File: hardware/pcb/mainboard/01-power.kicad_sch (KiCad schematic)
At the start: 42 parts, among them J1 BATTERIE JST-PH, J2 BOUTON contact JST-PH, J3 BOUTON LED JST-PH, Q1 AO3401A, Q2 2N7002, Q3 2N7002, SW1 QON, U2 BQ25896RTW, U3 TPS63001DRCR, U4 TPS61023DRL

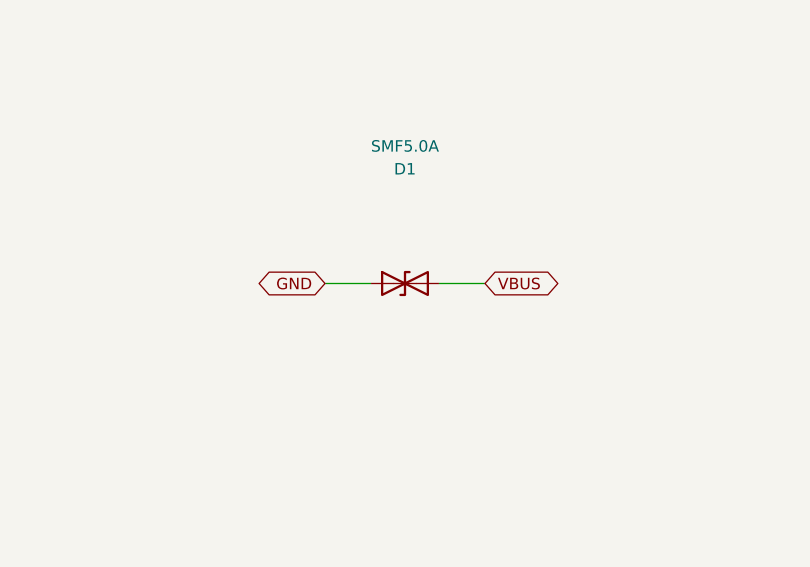
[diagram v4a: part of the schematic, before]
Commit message: fix(pcb): turn the VBUS TVS the right way round on both boards
D1 (SMF5.0A, unidirectional) carried Device:D_TVS, KiCad's bidirectional
symbol. Its pins are A1/A2, so no polarity is expressed, ERC has nothing to
reject, and the cathode landed wherever the wire ran — on GND. Plugging in
USB-C would have forward-biased the diode straight across VBUS, shorting the
port it protects.

Both boards now use Device:D_Zener, pin 1 = K, cathode on VBUS. The footprint
is rotated 180° so the symmetric SOD-123 pads keep the same copper: no track
moves, and DRC and unconnected counts are identical before and after.

check_pcb.py gains control H3 — every D<n> footprint must carry K/A pads. It
fails on the boards as they stood and passes 4/4 on the corrected ones.

Co-Authored-By: Claude Opus 5 (1M context) <noreply@anthropic.com>
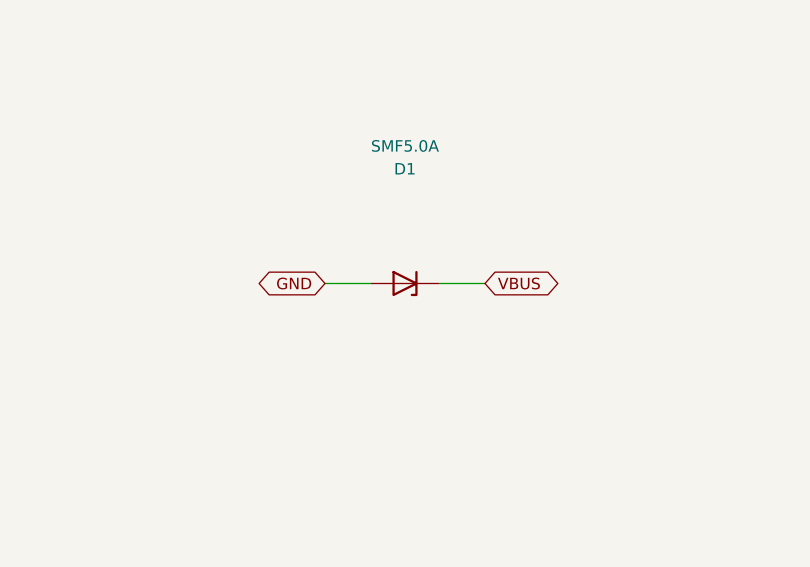
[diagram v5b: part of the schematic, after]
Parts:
- D1: symbol Device:D_TVS -> Device:D_Zener
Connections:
- net GND: now also D1.2 (A); no longer D1.1 (A1)
- net VBUS: now also D1.1 (K); no longer D1.2 (A2)
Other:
- moved on the sheet: D1
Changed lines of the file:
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@@
 	)
 	(symbol
-		(lib_id "Device:D_TVS")
-		(at 229.87 133.35 0)
+		(lib_id "Device:D_Zener")
+		(at 229.87 133.35 180)
 		(unit 1)
 		(body_style 1)
@@
 			)
 		)
-		(property "Description" ""
+		(property "Description" "TVS unidirectionnelle 5 V. Symbole zener parce que Device:D_TVS est bidirectionnel : ses broches A1/A2 n'expriment aucune polarité, et rien alors n'empêche la cathode d'atterrir sur GND."
 			(at 229.87 110.49 0)
 			(hide yes)
